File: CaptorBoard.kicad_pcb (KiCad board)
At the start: 2 copper layers, 90 x 50 mm, 51 parts, among them J1 Conn_01x06-Connector, J2 Screw_Terminal_01x03, J3 Screw_Terminal_01x03, J4 Conn_01x07, J5 Conn_01x04, K1 G5LE-1-DC5, K2 G5LE-1-DC5, Q1 2N7002E, Q2 2N7002E, SW1 SW_PUSH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

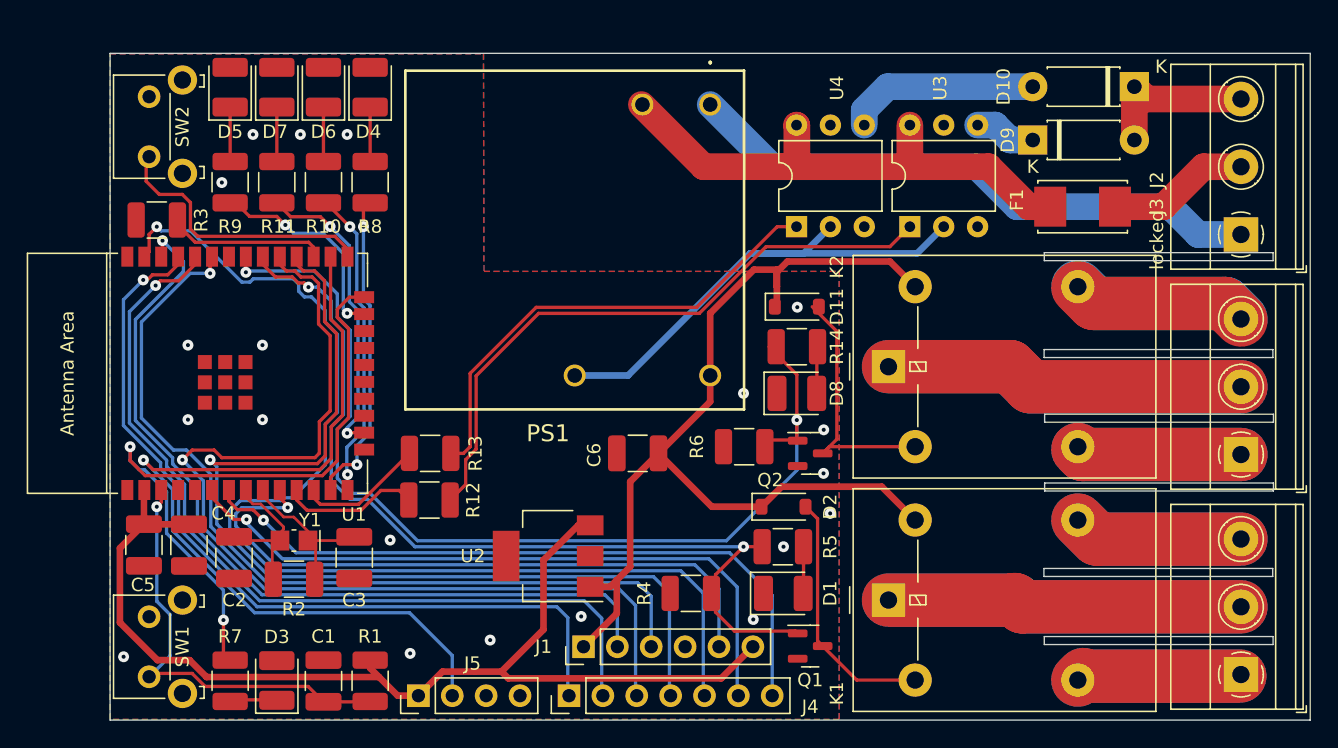
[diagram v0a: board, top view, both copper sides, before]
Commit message: route the new analog input and protections
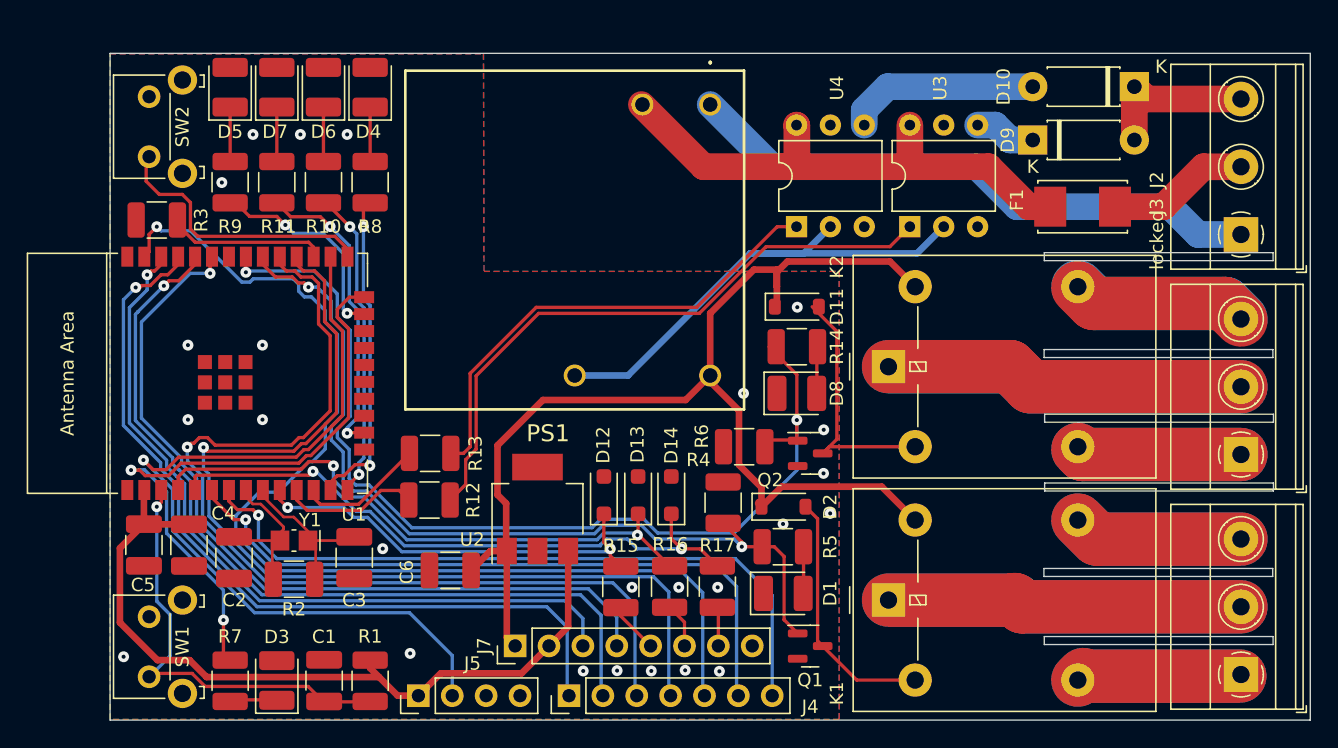
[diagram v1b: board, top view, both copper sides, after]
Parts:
- removed J1: Conn_01x06-Connector, Connector_PinHeader_2.54mm:PinHeader_1x06_P2.54mm_Vertical
- added D12: BZT52-C3V3, Diode_SMD:D_SOD-123F, F.Cu at (132.0, 83.1)
- added D13: BZT52-C3V3, Diode_SMD:D_SOD-123F, F.Cu at (134.6, 83.1)
- added D14: BZT52-C3V3, Diode_SMD:D_SOD-123F, F.Cu at (137.1, 83.1)
- added J7: Conn_01x08, Connector_PinHeader_2.54mm:PinHeader_1x08_P2.54mm_Vertical, F.Cu at (125.4, 94.4)
- added R15: 10k, Resistor_SMD:R_1210_3225Metric_Pad1.30x2.65mm_HandSolder, F.Cu at (133.3, 90.0)
- added R16: 10k, Resistor_SMD:R_1210_3225Metric_Pad1.30x2.65mm_HandSolder, F.Cu at (137.0, 90.0)
- added R17: 10k, Resistor_SMD:R_1210_3225Metric_Pad1.30x2.65mm_HandSolder, F.Cu at (140.5, 90.0)
- C1: value 0.1µ -> 1µ
- moved C6 16.6 mm to (120.5, 88.8)
- moved R4 7.22 mm to (141.0, 83.7), turned to 90 degrees
- moved U2 3.61 mm to (127.1, 84.2), turned to 90 degrees
- moved C1 0.06 mm to (111.0, 97.0)
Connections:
- U1 pad 10: /ANA -> /ANA0
- U1 pad 4: unconnected-(U1-SENSOR_VP/GPIO36/ADC1_CH0-Pad4) -> /ANA1
- U1 pad 5: unconnected-(U1-SENSOR_VN/GPIO39/ADC1_CH3-Pad5) -> /ANA2
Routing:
- net /ANA: track 49.1 -> 0.00 mm, vias 1 -> 0
- net /ANA2: track 0.00 -> 46.7 mm, vias 0 -> 2
- net /ANA1: track 0.00 -> 44.4 mm, vias 0 -> 2
- net /ANA0: track 0.00 -> 31.7 mm, vias 0 -> 2
- net +3.3V: track 81.5 -> 59.3 mm
- net +5V: track 75.5 -> 88.4 mm
- net /SCL_EXT: track 63.9 -> 57.9 mm
- net /POWER: track 51.1 -> 47.0 mm
- net Net-(J7-Pin_5): track 0.00 -> 3.80 mm
- net /SDA_EXT: track 65.0 -> 61.3 mm
- net Net-(J7-Pin_6): track 0.00 -> 3.36 mm
- net Net-(J7-Pin_7): track 0.00 -> 2.93 mm
- net /REL1: track 68.0 -> 66.0 mm
- net /GPIO5: track 75.8 -> 74.1 mm
- net /GPIO23: track 85.9 -> 84.3 mm
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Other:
- board text added: "1 - 5V 2 - 3.3V 3 - SDC 4 - SDA 5 - ANA0 6 - ANA1 7 - ANA2 8 - GND"
- board text removed: "1 - 5V 2 - SDC 3 - SDA 4 - GND 5 - Ana 6 - 3.3V"

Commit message: optimize route
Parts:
- removed J4: Conn_01x07, Connector_PinHeader_2.54mm:PinHeader_1x07_P2.54mm_Vertical
- J7: footprint Connector_PinHeader_2.54mm:PinHeader_1x08_P2.54mm_Vertical -> Connector_PinHeader_2.54mm:PinHeader_2x08_P2.54mm_Vertical
- moved C6 10.4 mm to (127.4, 80.9)
- moved J5 6.63 mm to (111.5, 98.0)
- moved R1 6.35 mm to (116.7, 91.1)
- moved C1 4.03 mm to (112.3, 93.2), turned to 180 degrees
- moved U2 3.67 mm to (126.7, 87.8), turned to -90 degrees
- moved J7 3.14 mm to (124.9, 97.5)
- moved SYM1 2.51 mm to (103.8, 76.2)
- moved D3 0.25 mm to (107.3, 96.9)
- moved R7 0.16 mm to (104.0, 96.9)
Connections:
- J7 pad 1: +5V -> +3.3V
- J7 pad 2: +3.3V -> +5V
- J7 pad 3: /SCL_EXT -> +5V
- J7 pad 4: /SDA_EXT -> /TX
- J7 pad 5: Net-(J7-Pin_5) -> /SCL_EXT
- J7 pad 6: Net-(J7-Pin_6) -> /RX
- J7 pad 7: Net-(J7-Pin_7) -> /SDA_EXT
- J7 pad 8: GND -> /GPIO34
- R15 pad 2: Net-(J7-Pin_5) -> Net-(J7-Pin_9)
- R16 pad 2: Net-(J7-Pin_6) -> Net-(J7-Pin_11)
- R17 pad 2: Net-(J7-Pin_7) -> Net-(J7-Pin_13)
- U1 pad 11: /PILOT_1 -> /GPIO26
- U1 pad 12: /PILOT_2 -> /GPIO27
- U1 pad 13: /CONF -> /PILOT_2
- U1 pad 14: /CONF-1°C -> /PILOT_1
- U1 pad 16: /CONF-2°C -> /REL1
- U1 pad 23: /ECO -> /REL2
- U1 pad 28: /GPIO17 -> /CONF
- U1 pad 29: /GPIO5 -> /CONF-1°C
- U1 pad 30: /REL1 -> /CONF-2°C
- U1 pad 31: /REL2 -> /ECO
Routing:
- net /GPIO17: track 74.7 -> 0.00 mm, vias 1 -> 0
- net /GPIO5: track 74.1 -> 0.00 mm, vias 1 -> 0
- net /GPIO27: track 0.00 -> 39.1 mm, vias 0 -> 1
- net /GPIO26: track 0.00 -> 38.7 mm, vias 0 -> 1
- net /CONF-2°C: track 22.7 -> 4.72 mm, vias 2 -> 0
- net /REL1: track 66.0 -> 48.3 mm
- net /CONF-1°C: track 23.4 -> 6.09 mm, vias 2 -> 0
- net /CONF: track 24.2 -> 7.46 mm, vias 2 -> 0
- net /GPIO23: track 84.3 -> 68.9 mm
- net Net-(U1-GPIO16): track 12.3 -> 27.5 mm
- net /GPIO35: track 53.1 -> 38.3 mm
- net /GPIO34: track 51.6 -> 37.0 mm
- net /ECO: track 16.0 -> 4.84 mm, vias 2 -> 0
- net /REL2: track 75.9 -> 65.0 mm
- net +3.3V: track 59.3 -> 69.7 mm
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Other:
- board text added: "1 - 3.3V 3 - 5V 5 - SDC 7 - SDA 9 - ANA0 11 - ANA1 13 - ANA2 15 - GND"
- board text added: "5V - 2 TX - 4 RX - 6 GPIO34 - 8 GPIO35 - 10 GPIO23 - 12 GPIO26 - 14 GPIO27 - 16"
- board text removed: "1 - 5V 2 - 3.3V 3 - SDC 4 - SDA 5 - ANA0 6 - ANA1 7 - ANA2 8 - GND"
- board text removed: "1 - TX 2 - RX 3 - GPIO5 4 - GPIO17 5 - GPIO23 6 - GPIO34 7 - GPIO35"

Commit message: change route
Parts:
- moved R15 0.80 mm to (132.5, 90.0)
- moved R16 0.46 mm to (136.5, 90.0)
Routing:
- net Net-(J7-Pin_9): track 7.95 -> 6.69 mm
- net Net-(J7-Pin_11): track 7.49 -> 6.70 mm
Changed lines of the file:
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@@
   )
   (footprint "Resistor_SMD:R_1210_3225Metric_Pad1.30x2.65mm_HandSolder" (layer "F.Cu")
-    (at 133.2992 90.017 -90)
+    (at 132.5 90.05 -90)
     (descr "Resistor SMD 1210 (3225 Metric), square (rectangular) end terminal, IPC_7351 nominal with elongated pad for handsoldering. (Body size source: IPC-SM-782 page 72, https://www.pcb-3d.com/wordpress/wp-content/uploads/ipc-sm-782a_amendment_1_and_2.pdf), generated with kicad-footprint-generator")
     (tags "resistor handsolder")
@@
   )
   (footprint "Resistor_SMD:R_1210_3225Metric_Pad1.30x2.65mm_HandSolder" (layer "F.Cu")
-    (at 136.9568 89.9916 -90)
+    (at 136.5 89.9916 -90)
     (descr "Resistor SMD 1210 (3225 Metric), square (rectangular) end terminal, IPC_7351 nominal with elongated pad for handsoldering. (Body size source: IPC-SM-782 page 72, https://www.pcb-3d.com/wordpress/wp-content/uploads/ipc-sm-782a_amendment_1_and_2.pdf), generated with kicad-footprint-generator")
     (tags "resistor handsolder")
@@
     (pts (xy 185 50) (xy 185 100))
     (height -3.5)
-    (gr_text "50,0000 mm" (at 187.35 75 90) (layer "B.Fab")
+    (gr_text "50.0000 mm" (at 187.35 75 90) (layer "B.Fab")
       (effects (font (size 1 1) (thickness 0.15)))
     )
@@
     (pts (xy 95 50) (xy 185 50))
     (height -4.5)
-    (gr_text "90,0000 mm" (at 140 44.35) (layer "B.Fab")
+    (gr_text "90.0000 mm" (at 140 44.35) (layer "B.Fab")
       (effects (font (size 1 1) (thickness 0.15)))
     )
@@
   (segment (start 131.2418 94.604299) (end 131.2418 96.266) (width 0.25) (layer "B.Cu") (net 22))
   (segment (start 106.578569 90.15) (end 124.520388 90.15) (width 0.25) (layer "B.Cu") (net 22))
+  (segment (start 132.5118 87.1562) (end 132.0292 86.6736) (width 0.25) (layer "F.Cu") (net 23))
+  (segment (start 132.0292 86.6736) (end 132.0292 84.5342) (width 0.25) (layer "F.Cu") (net 23))
+  (segment (start 132.5118 87.6796) (end 133.2992 88.467) (width 0.25) (layer "F.Cu") (net 23))
   (segment (start 108.947957 84.346917) (end 108.743917 84.346917) (width 0.25) (layer "F.Cu") (net 23))
   (segment (start 108.743917 84.346917) (end 107.723 83.326) (width 0.25) (layer "F.Cu") (net 23))
   (segment (start 114.642462 84.7962) (end 109.39724 84.7962) (width 0.25) (layer "F.Cu") (net 23))
   (segment (start 115.837331 85.991069) (end 114.642462 84.7962) (width 0.25) (layer "F.Cu") (net 23))
-  (segment (start 132.5118 87.6796) (end 133.2992 88.467) (width 0.25) (layer "F.Cu") (net 23))
   (segment (start 107.723 83.326) (end 107.723 82.746) (width 0.25) (layer "F.Cu") (net 23))
-  (segment (start 132.0292 84.5342) (end 132.0292 86.6736) (width 0.25) (layer "F.Cu") (net 23))
   (segment (start 132.5118 87.1562) (end 132.5118 87.6796) (width 0.25) (layer "F.Cu") (net 23))
   (segment (start 109.39724 84.7962) (end 108.947957 84.346917) (width 0.25) (layer "F.Cu") (net 23))
-  (segment (start 132.0292 86.6736) (end 132.5118 87.1562) (width 0.25) (layer "F.Cu") (net 23))
   (via (at 115.837331 85.991069) (size 0.82) (drill 0.3) (layers "F.Cu" "B.Cu") (net 23))
   (via (at 132.5118 87.1562) (size 0.82) (drill 0.3) (layers "F.Cu" "B.Cu") (net 23))
-  (segment (start 116.822481 85.991069) (end 118.207412 87.376) (width 0.25) (layer "B.Cu") (net 23))
-  (segment (start 132.292 87.376) (end 132.5118 87.1562) (width 0.25) (layer "B.Cu") (net 23))
-  (segment (start 115.837331 85.991069) (end 116.822481 85.991069) (width 0.25) (layer "B.Cu") (net 23))
-  (segment (start 118.207412 87.376) (end 132.292 87.376) (width 0.25) (layer "B.Cu") (net 23))
+  (segment (start 132.292 87.376) (end 118.207412 87.376) (width 0.25) (layer "B.Cu") (net 23))
+  (segment (start 118.207412 87.376) (end 116.822481 85.991069) (width 0.25) (layer "B.Cu") (net 23))
+  (segment (start 132.5118 87.1562) (end 132.292 87.376) (width 0.25) (layer "B.Cu") (net 23))
+  (segment (start 116.822481 85.991069) (end 115.837331 85.991069) (width 0.25) (layer "B.Cu") (net 23))
   (segment (start 99.469161 80.9498) (end 100.133261 80.2857) (width 0.25) (layer "F.Cu") (net 24))
   (segment (start 112.4276 70.821843) (end 111.533 69.927243) (width 0.25) (layer "F.Cu") (net 24))
@@
   (segment (start 110.758 64.171) (end 110.263 64.666) (width 0.25) (layer "F.Cu") (net 35))
   (segment (start 109.906153 80.6157) (end 109.336153 81.1857) (width 0.25) (layer "F.Cu") (net 36))
-  (segment (start 134.646953 86.131753) (end 134.543447 86.131753) (width 0.25) (layer "F.Cu") (net 36))
   (segment (start 100.103 81.746) (end 100.103 82.746) (width 0.25) (layer "F.Cu") (net 36))
   (segment (start 100.6633 81.1857) (end 100.103 81.746) (width 0.25) (layer "F.Cu") (net 36))
   (segment (start 109.336153 81.1857) (end 100.6633 81.1857) (width 0.25) (layer "F.Cu") (net 36))
   (segment (start 134.5946 86.0806) (end 134.543447 86.131753) (width 0.25) (layer "F.Cu") (net 36))
-  (segment (start 136.9568 88.4416) (end 134.646953 86.131753) (width 0.25) (layer "F.Cu") (net 36))
   (segment (start 134.5946 84.5312) (end 134.5946 86.0806) (width 0.25) (layer "F.Cu") (net 36))
   (segment (start 111.746071 80.9365) (end 111.425271 80.6157) (width 0.25) (layer "F.Cu") (net 36))
+  (segment (start 134.646953 86.131753) (end 134.543447 86.131753) (width 0.25) (layer "F.Cu") (net 36))
   (segment (start 111.425271 80.6157) (end 109.906153 80.6157) (width 0.25) (layer "F.Cu") (net 36))
+  (segment (start 136.9568 88.4416) (end 134.646953 86.131753) (width 0.25) (layer "F.Cu") (net 36))
   (via (at 111.746071 80.9365) (size 0.82) (drill 0.3) (layers "F.Cu" "B.Cu") (net 36))
   (via (at 134.543447 86.131753) (size 0.82) (drill 0.3) (layers "F.Cu" "B.Cu") (net 36))
@@
   (segment (start 132.290481 92.471) (end 135.461293 92.471) (width 0.25) (layer "B.Cu") (net 65))
   (segment (start 135.461293 92.471) (end 136.317093 93.3268) (width 0.25) (layer "B.Cu") (net 65))
-  (segment (start 135.405447 97.536) (end 135.0518 97.536) (width 0.25) (layer "F.Cu") (net 66))
-  (segment (start 136.3202 94.588) (end 136.3202 96.621247) (width 0.25) (layer "F.Cu") (net 66))
-  (segment (start 133.2992 91.567) (end 136.3202 94.588) (width 0.25) (layer "F.Cu") (net 66))
-  (segment (start 136.3202 96.621247) (end 135.405447 97.536) (width 0.25) (layer "F.Cu") (net 66))
-  (segment (start 137.894647 97.536) (end 137.5918 97.536) (width 0.25) (layer "F.Cu") (net 67))
-  (segment (start 138.8602 93.445) (end 138.8602 96.570447) (width 0.25) (layer "F.Cu") (net 67))
-  (segment (start 138.8602 96.570447) (end 137.894647 97.536) (width 0.25) (layer "F.Cu") (net 67))
-  (segment (start 136.9568 91.5416) (end 138.8602 93.445) (width 0.25) (layer "F.Cu") (net 67))
-  (segment (start 140.536247 97.536) (end 140.1318 97.536) (width 0.25) (layer "F.Cu") (net 68))
-  (segment (start 140.5382 91.5416) (end 141.4256 92.429) (width 0.25) (layer "F.Cu") (net 68))
+  (segment (start 133.2992 93.7992) (end 133.8768 94.3768) (width 0.25) (layer "F.Cu") (net 66))
+  (segment (start 133.8768 96.361) (end 135.0518 97.536) (width 0.25) (layer "F.Cu") (net 66))
+  (segment (start 133.8768 94.3768) (end 133.8768 96.361) (width 0.25) (layer "F.Cu") (net 66))
+  (segment (start 133.2992 91.567) (end 133.2992 93.7992) (width 0.25) (layer "F.Cu") (net 66))
+  (segment (start 137.5918 96.657701) (end 137.5918 97.536) (width 0.25) (layer "F.Cu") (net 67))
+  (segment (start 136.4168 95.482701) (end 137.5918 96.657701) (width 0.25) (layer "F.Cu") (net 67))
+  (segment (start 136.4168 92.0816) (end 136.4168 95.482701) (width 0.25) (layer "F.Cu") (net 67))
+  (segment (start 136.9568 91.5416) (end 136.4168 92.0816) (width 0.25) (layer "F.Cu") (net 67))
+  (segment (start 141.4256 94.4256) (end 141.4256 96.646647) (width 0.25) (layer "F.Cu") (net 68))
+  (segment (start 140.5 93.5) (end 141.4256 94.4256) (width 0.25) (layer "F.Cu") (net 68))
   (segment (start 141.4256 96.646647) (end 140.536247 97.536) (width 0.25) (layer "F.Cu") (net 68))
-  (segment (start 141.4256 92.429) (end 141.4256 96.646647) (width 0.25) (layer "F.Cu") (net 68))
+  (segment (start 140.5 91.5798) (end 140.5 93.5) (width 0.25) (layer "F.Cu") (net 68))
+  (segment (start 140.5382 91.5416) (end 140.5 91.5798) (width 0.25) (layer "F.Cu") (net 68))
+  (segment (start 140.536247 97.536) (end 140.1318 97.536) (width 0.25) (layer "F.Cu") (net 68))
   (zone (net 9) (net_name "GND") (layers "F&B.Cu") (hatch edge 0.508)
     (priority 3)
